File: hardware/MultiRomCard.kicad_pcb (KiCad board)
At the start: 2 copper layers, 125 x 100 mm, 18 parts, among them P1 VC4000_Cartridge_Bus, P2 MicroSD_Breakout, P3 Test Header, U1 Arduino_Nano, U2 74HC595, U3 74HC595, U4 74HC595, U5 6264, U6 74HC245, U7 74HC245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

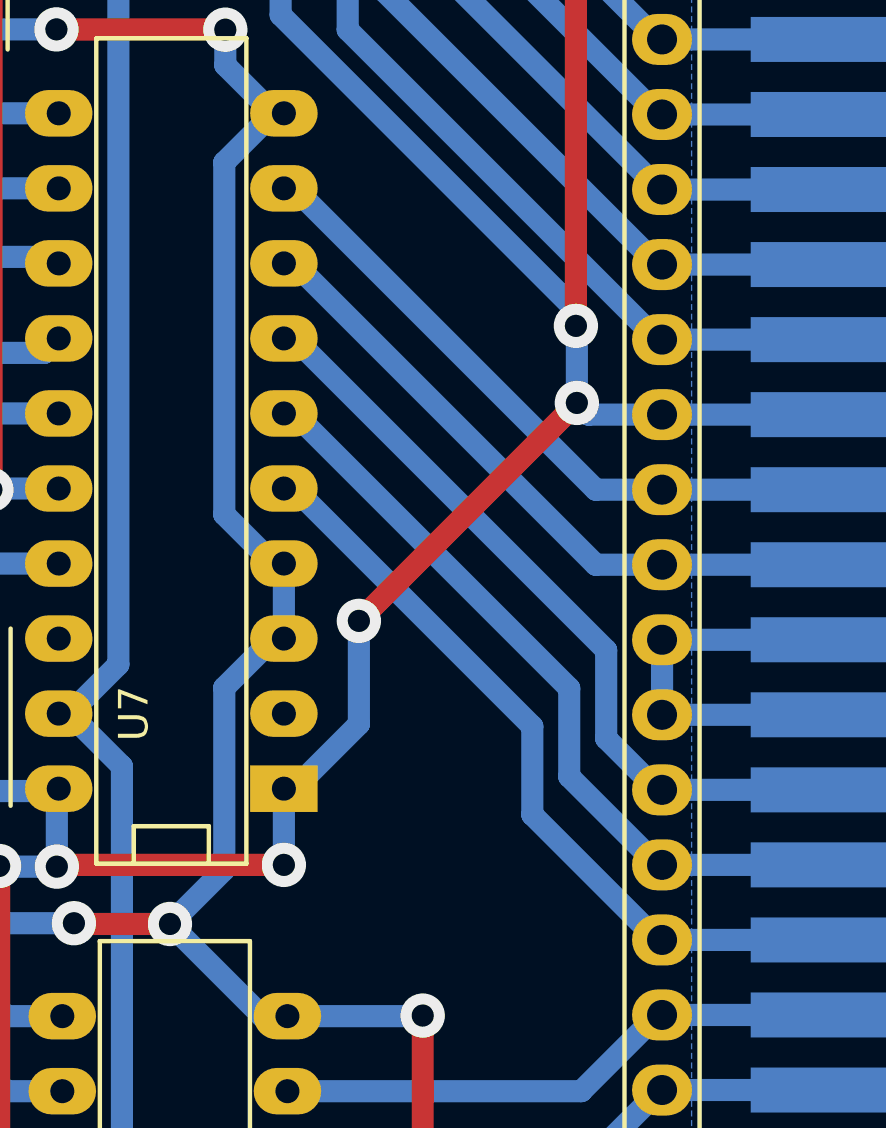
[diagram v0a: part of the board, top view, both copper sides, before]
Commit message: [SCH/PCB] A12+PVI_SEL needs to be connected to /CE1.
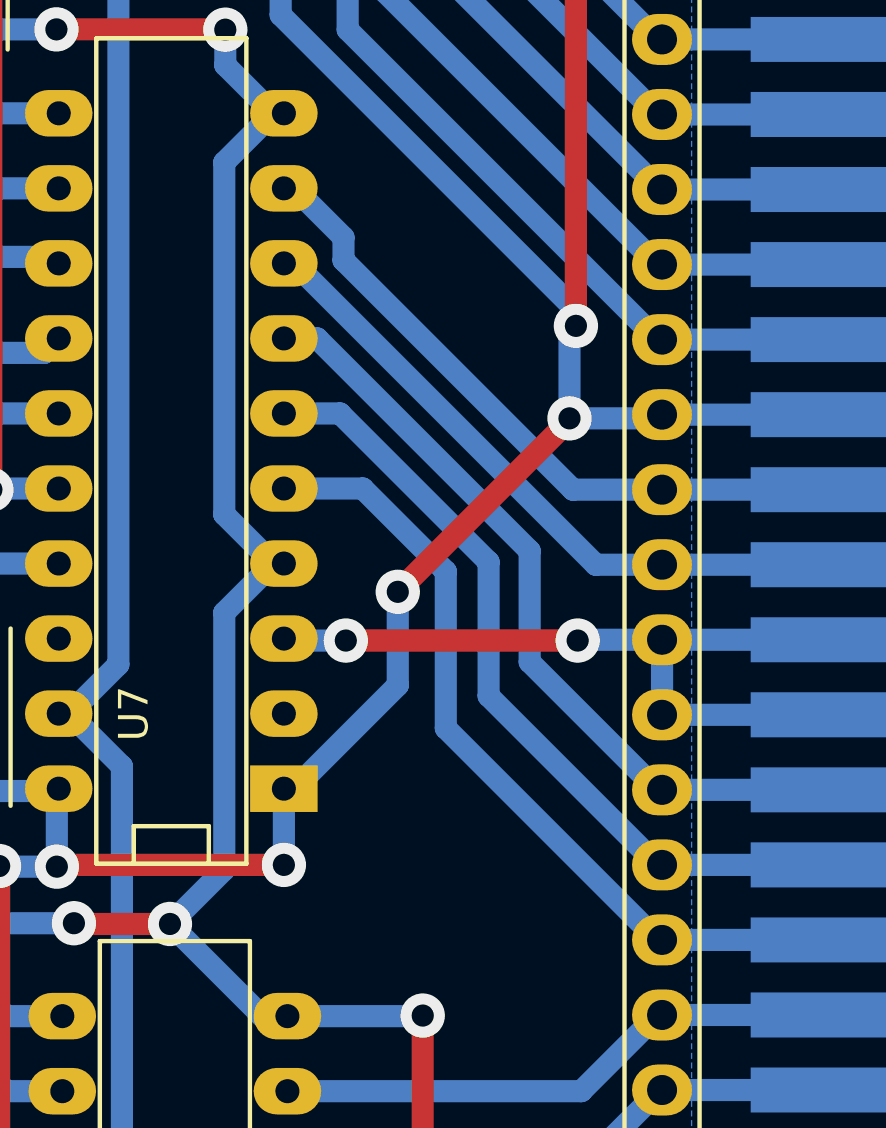
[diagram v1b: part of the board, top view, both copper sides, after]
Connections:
- U7 pad 3: GND -> /EA12
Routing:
- net /EA12: track 22.5 -> 35.6 mm, vias 0 -> 2
- net /EA11: track 30.9 -> 32.2 mm
- net /EA10: track 30.9 -> 31.8 mm

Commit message: [SCH/PCB] Rotate MicroSD breakout header.
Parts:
- moved P2 10.7 mm to (91.3, 92.5), turned to 180 degrees
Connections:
- U1 pad 13: Net-(P2-Pad4) -> Net-(P2-Pad1)
- U1 pad 15: Net-(P2-Pad2) -> Net-(P2-Pad4)
- U1 pad 16: Net-(P2-Pad1) -> Net-(P2-Pad2)
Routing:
- net VCC: track 440.8 -> 430.4 mm
- net Net-(P2-Pad2): track 22.8 -> 12.9 mm
- net GND: track 516.2 -> 512.5 mm
- net Net-(P2-Pad1): track 22.6 -> 22.1 mm, vias 2 -> 0
- net Net-(P2-Pad3): track 23.2 -> 22.7 mm

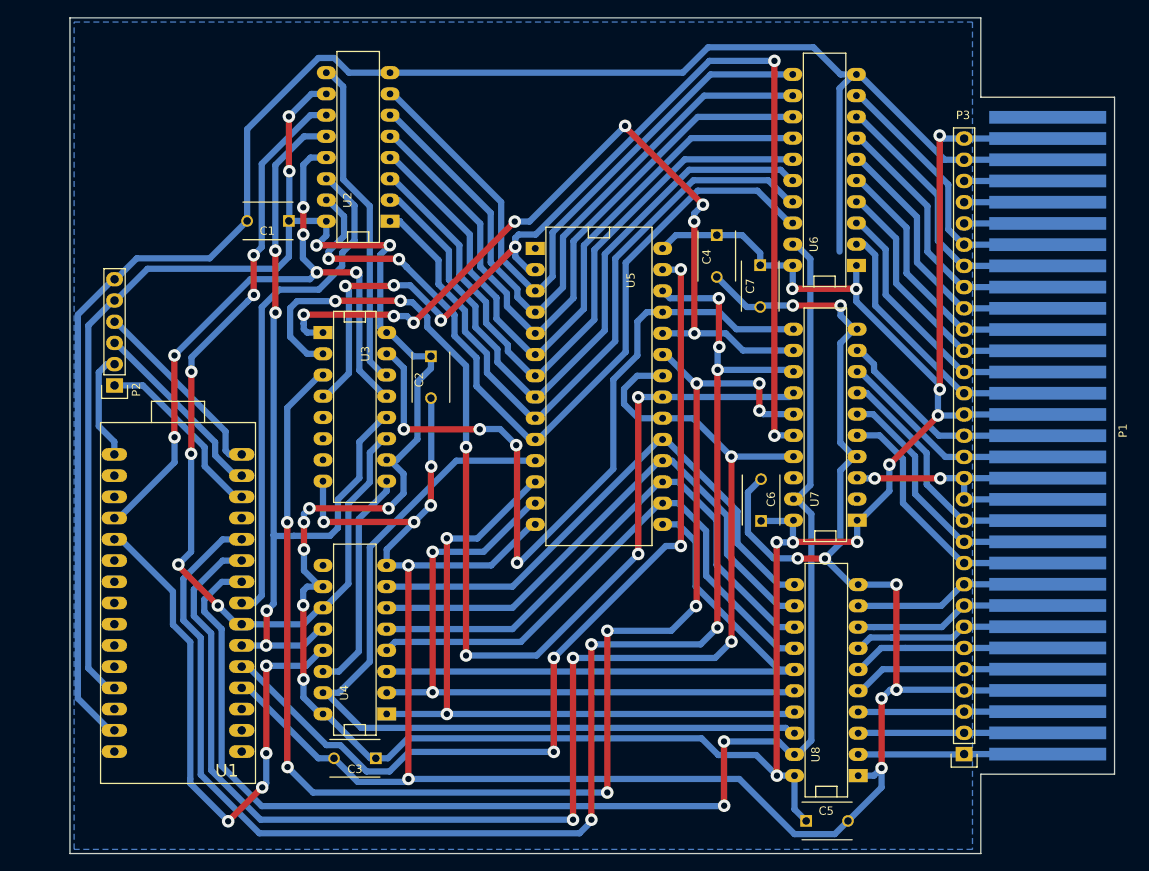
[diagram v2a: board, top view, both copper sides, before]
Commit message: [HW/FW] Incorporate latest changes into hardware and firmware.
- From now on, we should call the hardware rev. 0.2.
- All games should now work (ROM and ROM+RAM)
- Up to 6K (5.5K) ROM is currently allowed (7.5K should be
  possible, too, with one line change in the FW.)
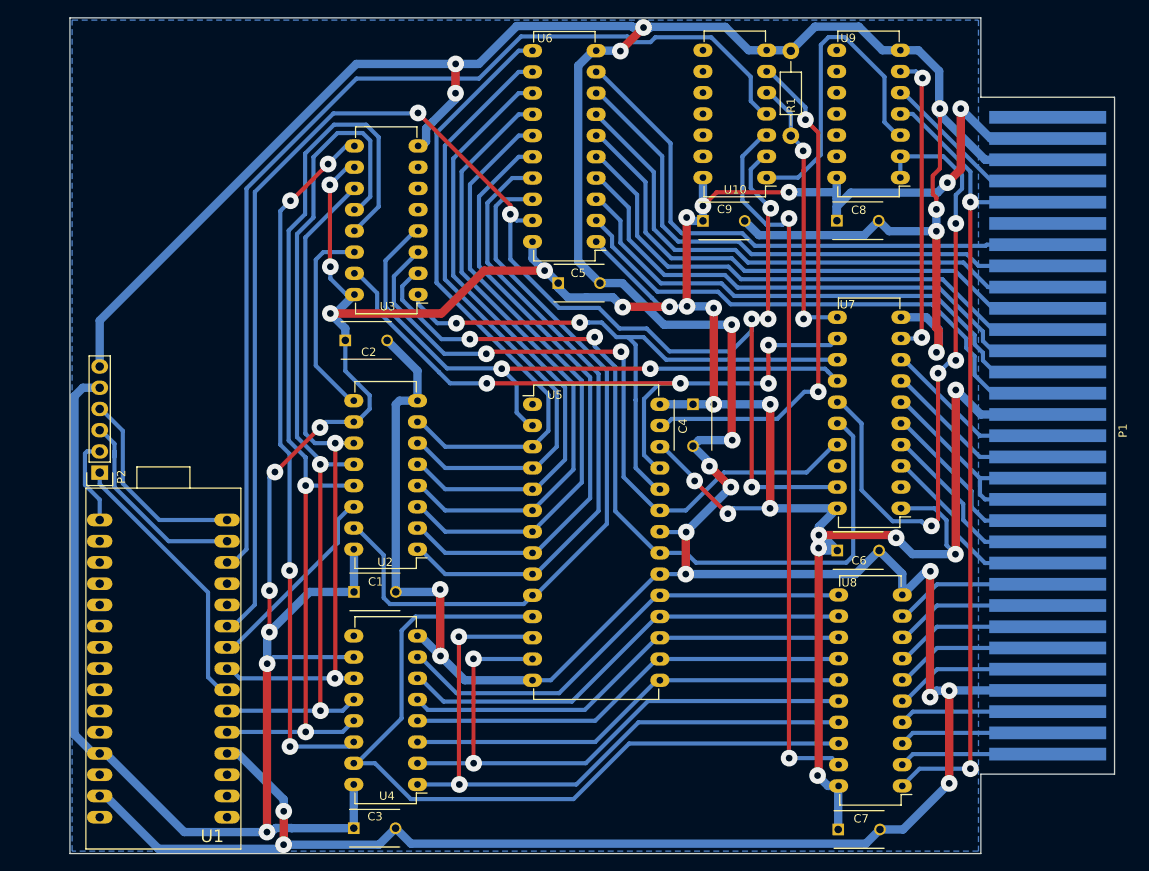
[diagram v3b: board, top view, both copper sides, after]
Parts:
- removed P3: Test Header, Pin_Headers:Pin_Header_Straight_1x30
- added C8: .1uF, Capacitors_ThroughHole:C_Disc_D6_P5, F.Cu at (177.8, 72.8)
- added C9: .1uF, Capacitors_ThroughHole:C_Disc_D6_P5, F.Cu at (161.7, 72.8)
- added R1: 10k, Resistors_ThroughHole:Resistor_Horizontal_RM10mm, F.Cu at (172.3, 57.5)
- added U10: 74HC32, Housings_DIP:DIP-14_W7.62mm_LongPads, F.Cu at (169.4, 67.6)
- added U9: 74HC00, Housings_DIP:DIP-14_W7.62mm_LongPads, F.Cu at (185.4, 67.6)
- U2, U3, U4: footprint Housings_DIP:DIP-16__300_ELL -> Housings_DIP:DIP-16_W7.62mm_LongPads
- U5: footprint Housings_DIP:DIP-28__600_ELL -> Housings_DIP:DIP-28_W15.24mm_LongPads
- U6, U7, U8: footprint Housings_DIP:DIP-20__300_ELL -> Housings_DIP:DIP-20_W7.62mm_LongPads
- moved C5 70.9 mm to (144.4, 80.2)
- moved C7 68.2 mm to (177.9, 145.6), turned to 0 degrees
- moved U2 48.7 mm to (127.6, 112.1), turned to 180 degrees
- moved C1 45.1 mm to (120.0, 117.2), turned to 0 degrees
- moved U6 28.6 mm to (149.0, 75.3), turned to 180 degrees
- moved C4 20.4 mm to (160.6, 94.7)
- moved U4 18.9 mm to (127.6, 140.2), turned to 180 degrees
- moved U8 15.6 mm to (185.6, 140.4), turned to 180 degrees
- moved U3 15.4 mm to (127.7, 81.6), turned to 180 degrees
- moved U7 13.5 mm to (185.4, 107.2), turned to 180 degrees
- moved P2 10.6 mm to (89.6, 102.9)
- moved C2 10.4 mm to (119.0, 87.1), turned to 0 degrees
- moved C6 9.79 mm to (177.8, 112.2), turned to 0 degrees
- moved C3 8.77 mm to (120.0, 145.5), turned to 0 degrees
- moved U5 8.23 mm to (141.4, 94.7), turned to 0 degrees
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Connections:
- P1 pad 12: /CE2 -> /CE1
- P1 pad 26: /P26 -> Net-(P1-Pad26)
- P1 pad 27: /P27 -> /RW
- P1 pad 28: /P28 -> /WRP
- U1 pad 10: CE1SRAM -> OEVCBUS
- U1 pad 11: CE2SRAM -> Net-(U1-Pad11)
- U1 pad 13: Net-(P2-Pad1) -> WESRAM
- U1 pad 5: WESRAM -> Net-(U1-Pad5)
- U1 pad 7: Net-(U1-Pad7) -> Net-(P2-Pad1)
- U1 pad 9: OEVCBUS -> Net-(U1-Pad9)
- U2 pad 11: Net-(U1-Pad7) -> Net-(U1-Pad8)
- U2 pad 13: Net-(U1-Pad19) -> Net-(U1-Pad5)
- U2 pad 14: Net-(U1-Pad8) -> Net-(U1-Pad9)
- U3 pad 11: Net-(U1-Pad7) -> Net-(U1-Pad8)
- U3 pad 13: Net-(U1-Pad19) -> Net-(U1-Pad5)
- U4 pad 11: Net-(U1-Pad7) -> Net-(U1-Pad8)
- U4 pad 13: Net-(U1-Pad20) -> Net-(U1-Pad5)
- U5 pad 20: CE1SRAM -> GND
- U5 pad 22: CE1SRAM -> GND
- U5 pad 26: CE2SRAM -> VCC
- U5 pad 27: WESRAM -> Net-(U10-Pad6)
- U7 pad 11: /A8 -> Net-(R1-Pad1)
- U7 pad 12: /A9 -> /A8
- U7 pad 13: CE2SRAM -> /A9
- U7 pad 14: /A10 -> /A12
- U7 pad 15: /A11 -> Net-(U7-Pad15)
- U7 pad 16: /A12 -> /A10
- U7 pad 17: CE1SRAM -> /A11
- U7 pad 3: /EA12 -> /EA11
- U7 pad 4: GND -> /EA10
- U7 pad 5: /EA11 -> /CE1
- U7 pad 6: /EA10 -> /EA12
- U7 pad 7: /CE2 -> /EA9
- U7 pad 8: /EA9 -> /EA8
- U7 pad 9: /EA8 -> WCONTROL
- U8 pad 1: GND -> /RW
- U8 pad 19: OEVCBUS -> CEDBUS
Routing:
- net CE2SRAM: track 176.4 -> 0.00 mm, vias 6 -> 0
- net CE1SRAM: track 166.6 -> 0.00 mm, vias 4 -> 0
- net Net-(U1-Pad5): track 0.00 -> 115.6 mm, vias 0 -> 2
- net Net-(U1-Pad7): track 107.2 -> 0.00 mm, vias 6 -> 0
- net /RW: track 0.00 -> 101.0 mm, vias 0 -> 2
- net GND: track 512.5 -> 603.8 mm, vias 14 -> 22
- net VCC: track 430.4 -> 520.2 mm, vias 20 -> 30
- net CEDBUS: track 0.00 -> 87.2 mm, vias 0 -> 2
- net /A11: track 167.3 -> 83.1 mm, vias 8 -> 2
- net Net-(U1-Pad19): track 81.8 -> 0.00 mm, vias 6 -> 0
- net Net-(U7-Pad15): track 0.00 -> 76.8 mm, vias 0 -> 4
- net Net-(U1-Pad20): track 67.9 -> 0.00 mm, vias 4 -> 0
- net Net-(U10-Pad6): track 0.00 -> 61.7 mm, vias 0 -> 2
- net Net-(U3-Pad9): track 27.0 -> 84.5 mm, vias 0 -> 4
- net /A12: track 133.2 -> 77.2 mm, vias 6 -> 2
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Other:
- net class Default: trace_width 0.75 -> 0.5; via_dia 1.5 -> 2; via_drill 0.75 -> 0.8
- net class Power: trace_width 1.5 -> 1; via_drill 1.5 -> 1

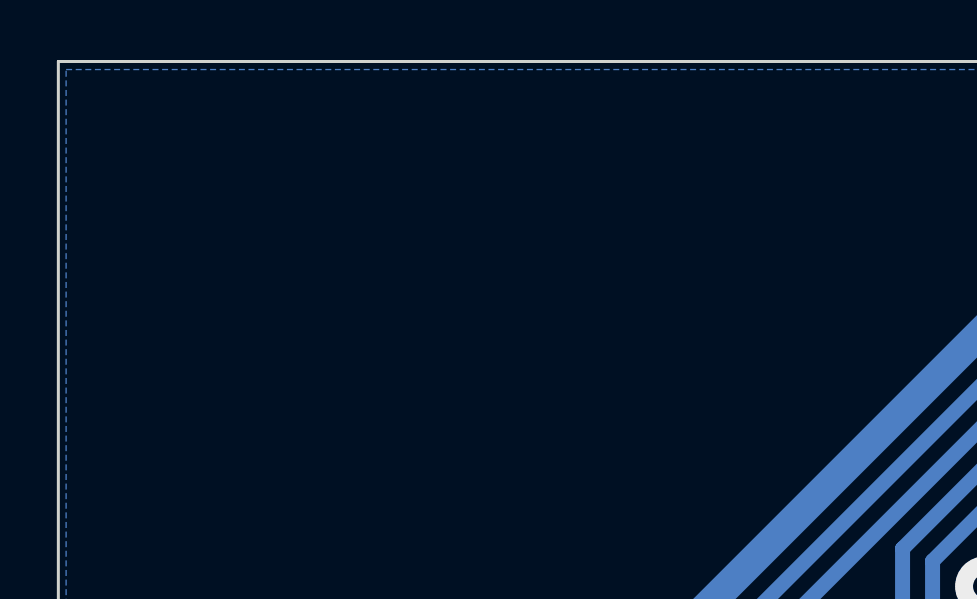
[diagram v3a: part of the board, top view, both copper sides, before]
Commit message: version string added on copper side
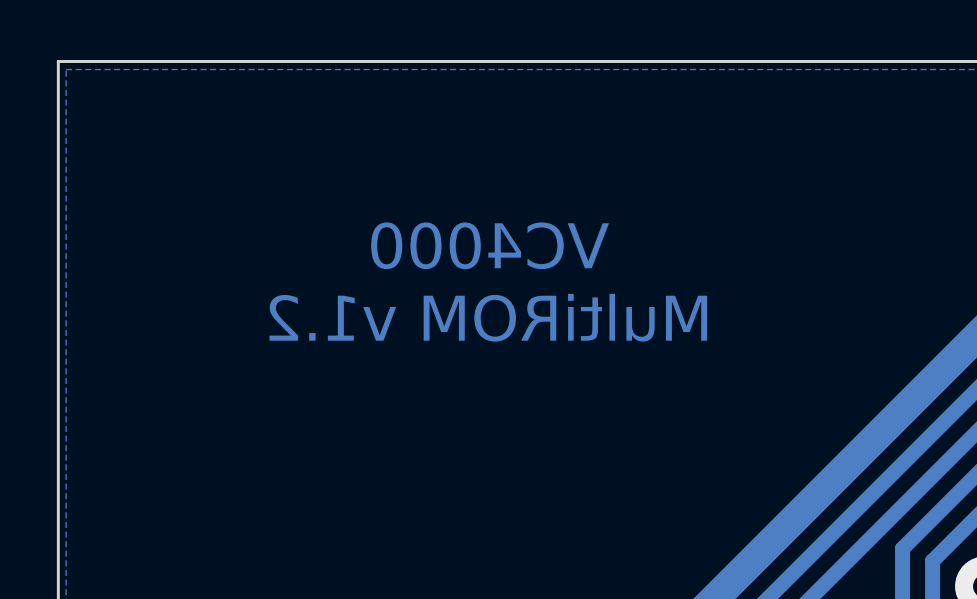
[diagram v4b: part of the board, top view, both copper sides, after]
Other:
- board text added: "VC4000 MultiROM v1.2"

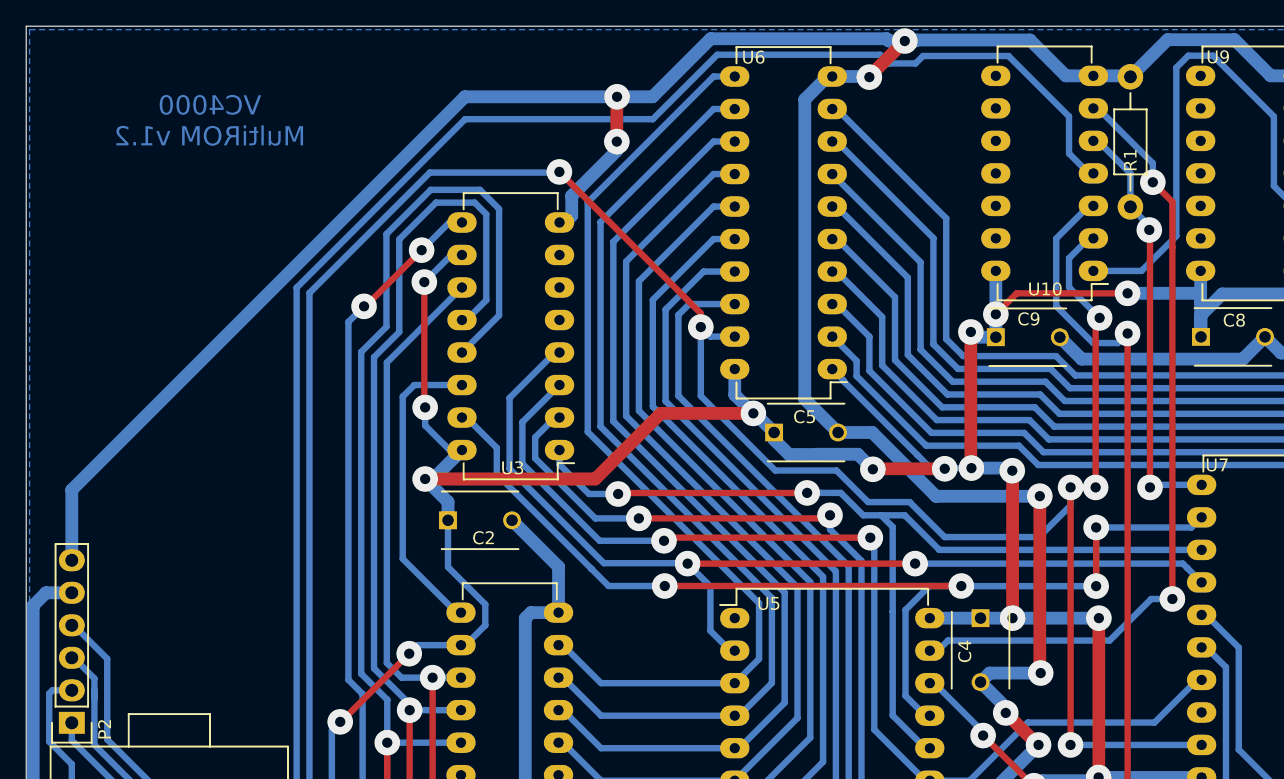
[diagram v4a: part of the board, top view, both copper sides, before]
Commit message: [HW] A little cleanup on the schematic, new PDF printouts.
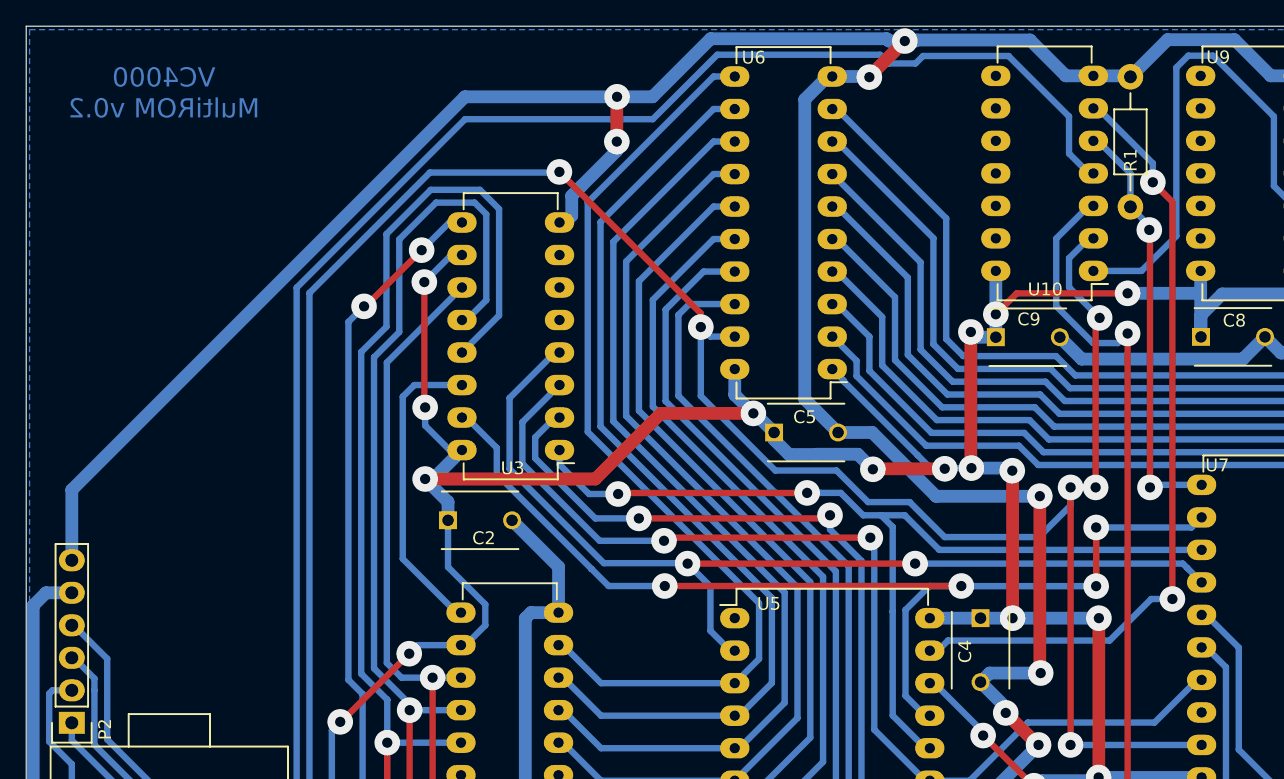
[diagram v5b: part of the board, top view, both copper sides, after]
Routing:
- net Net-(P2-Pad3): track 24.4 -> 23.8 mm
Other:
- board text added: "VC4000 MultiROM v0.2"
- board text removed: "VC4000 MultiROM v1.2"
